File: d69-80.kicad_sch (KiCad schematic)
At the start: 163 parts, among them SW1 SW_Push, SW10 SW_Push, SW101 SW_SPST, SW11 SW_Push, SW12 SW_Push, SW13 SW_Push, SW14 SW_Push, SW15 SW_Push, SW16 SW_Push, SW17 SW_Push, SW18 SW_Push, SW19 SW_Push, SW2 SW_Push, SW20 SW_Push, SW21 SW_Push, SW22 SW_Push, SW23 SW_Push, SW24 SW_Push, SW25 SW_Push, SW26 SW_Push, SW27 SW_Push, SW28 SW_Push, SW29 SW_Push, SW3 SW_Push, SW30 SW_Push, SW31 SW_Push, SW32 SW_Push, SW33 SW_Push, SW34 SW_Push, SW35 SW_Push, SW36 SW_Push, SW37 SW_Push, SW38 SW_Push, SW39 SW_Push, SW4 SW_Push, SW40 SW_Push, SW41 SW_Push, SW42 SW_Push, SW43 SW_Push, SW44 SW_Push, SW45 SW_Push, SW46 SW_Push, SW47 SW_Push, SW48 SW_Push, SW49 SW_Push, SW5 SW_Push, SW50 SW_Push, SW51 SW_Push, SW52 SW_Push, SW53 SW_Push, SW54 SW_Push, SW55 SW_Push, SW56 SW_Push, SW57 SW_Push, SW58 SW_Push, SW59 SW_Push, SW6 SW_Push, SW60 SW_Push, SW61 SW_Push, SW62 SW_Push, SW63 SW_Push, SW64 SW_Push, SW65 SW_Push, SW66 SW_Push, SW67 SW_Push, SW68 SW_Push, SW69 SW_Push, SW7 SW_Push, SW70 SW_Push, SW71 SW_Push, SW72 SW_Push, SW73 SW_Push, SW74 SW_Push, SW75 SW_Push, SW76 SW_Push, SW77 SW_Push, SW78 SW_Push, SW79 SW_Push, SW8 SW_Push, SW80 SW_Push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

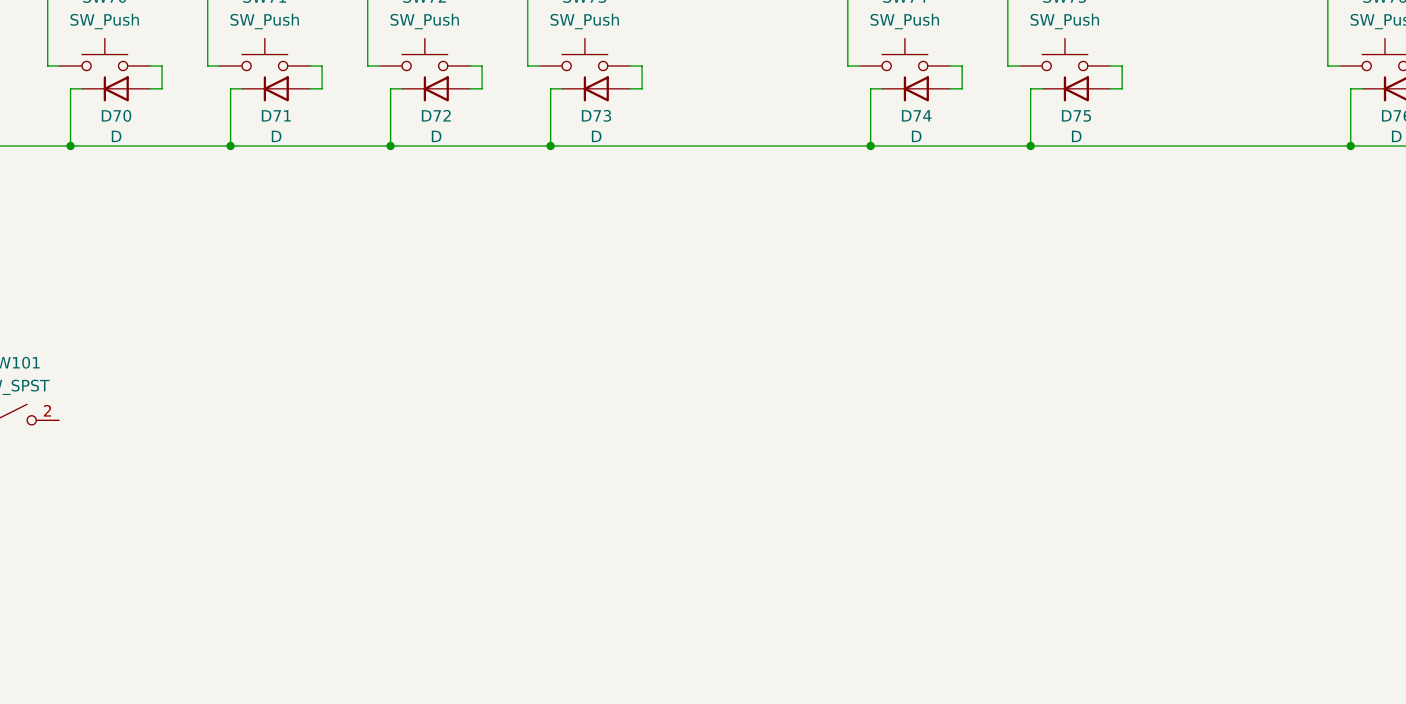
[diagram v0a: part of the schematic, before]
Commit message: adds mcu and io-expander, initial wiring
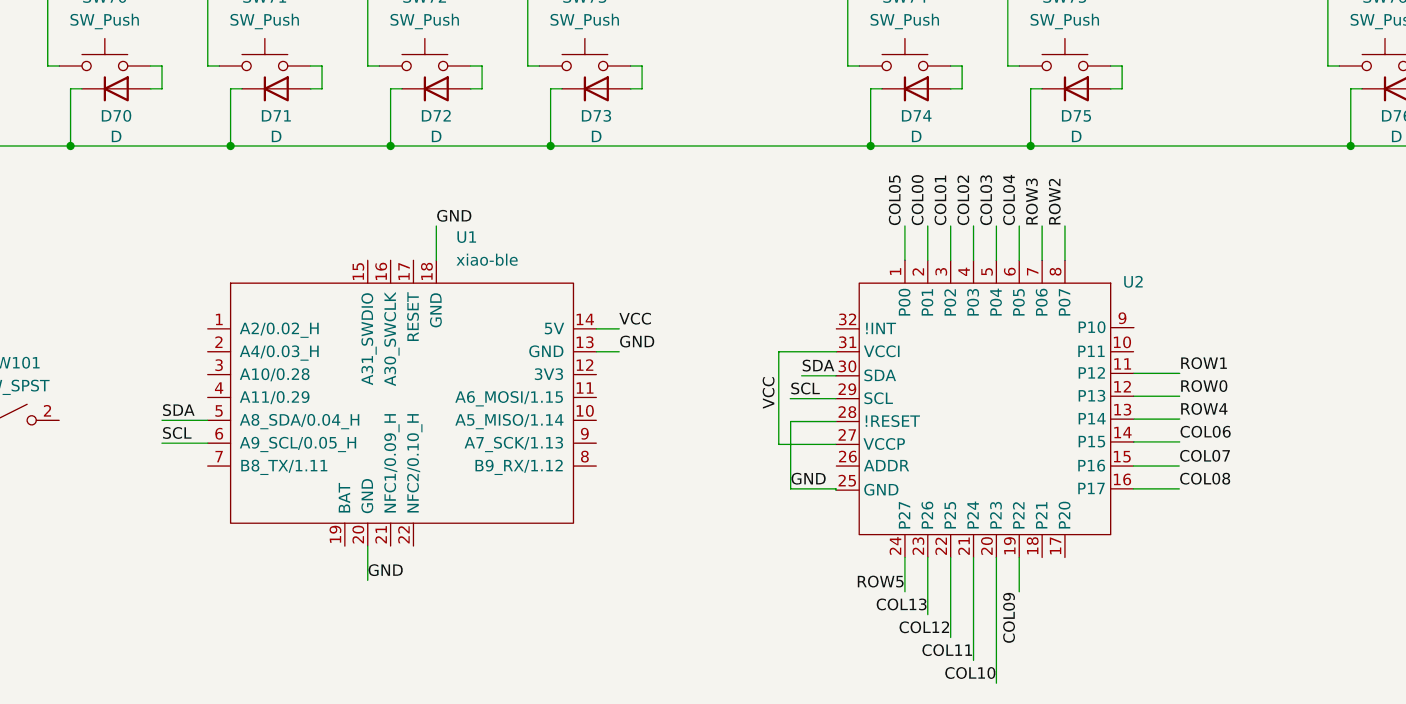
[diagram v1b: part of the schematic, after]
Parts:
- added U1: xiao-ble, Library:xiao-ble-smd-cutout, symbol Library:xiao-ble
- added U2: ~, Library:QFN-32_EP_5x5_Pitch0.5mm, symbol Library:TCA6424
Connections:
- net COL00: now also U2.2 (P01)
- net COL01: now also U2.3 (P02)
- net COL02: now also U2.4 (P03)
- net COL03: now also U2.5 (P04)
- net COL04: now also U2.6 (P05)
- net COL05: now also U2.1 (P00)
- net COL06: now also U2.14 (P15)
- net COL07: now also U2.15 (P16)
- net COL08: now also U2.16 (P17)
- net COL09: now also U2.19 (P22)
- net COL10: now also U2.20 (P23)
- net COL11: now also U2.21 (P24)
- net COL12: now also U2.22 (P25)
- net COL13: now also U2.23 (P26)
- net ROW0: now also U2.12 (P13)
- net ROW1: now also U2.11 (P12)
- net ROW2: now also U2.8 (P07)
- net ROW3: now also U2.7 (P06)
- net ROW4: now also U2.13 (P14)
- net ROW5: now also U2.24 (P27)
- new net GND: U1.13 (GND), U1.18 (GND), U1.20 (GND), U2.25 (GND), U2.28 (!RESET)
- new net SCL: U1.6 (A9_SCL/0.05_H), U2.29 (SCL)
- new net SDA: U1.5 (A8_SDA/0.04_H), U2.30 (SDA)
- new net VCC: U1.14 (5V), U2.27 (VCCP), U2.31 (VCCI)

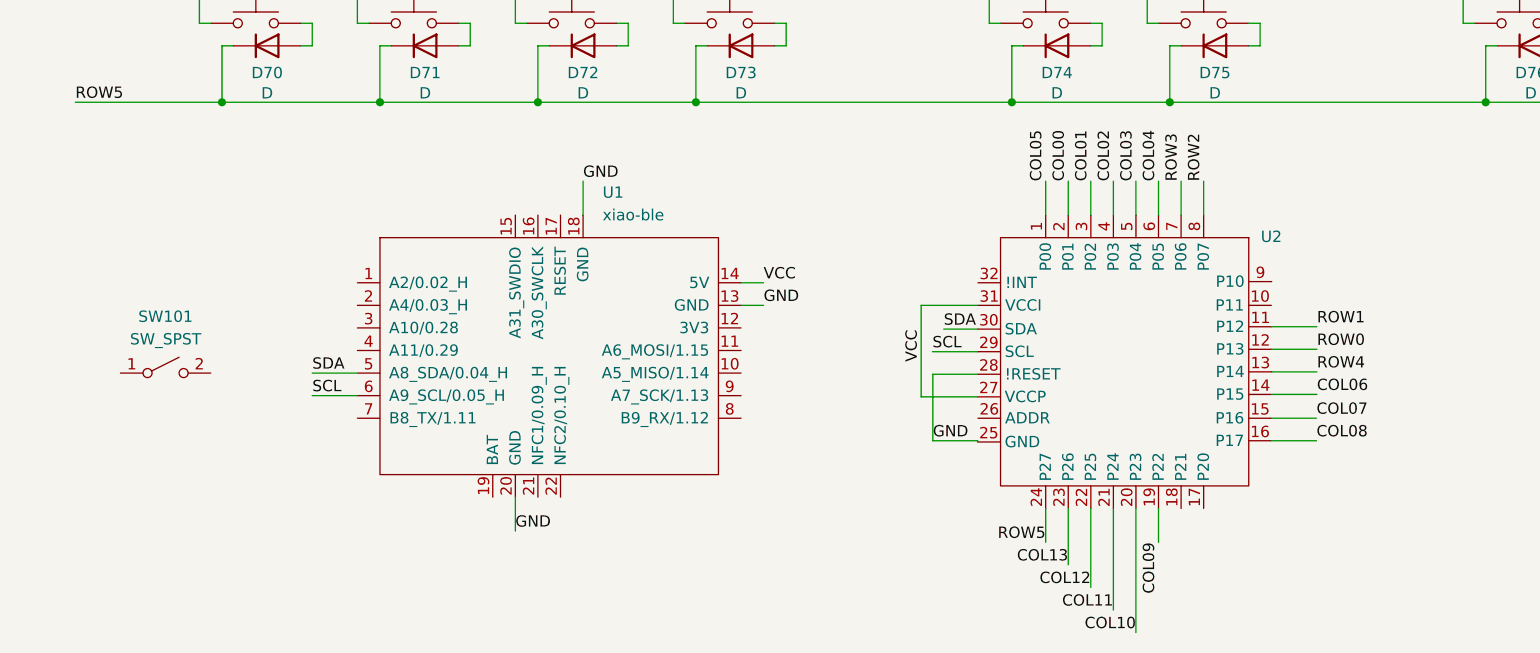
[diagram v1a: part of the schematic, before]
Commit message: adds leds, connects switch and some cleanup
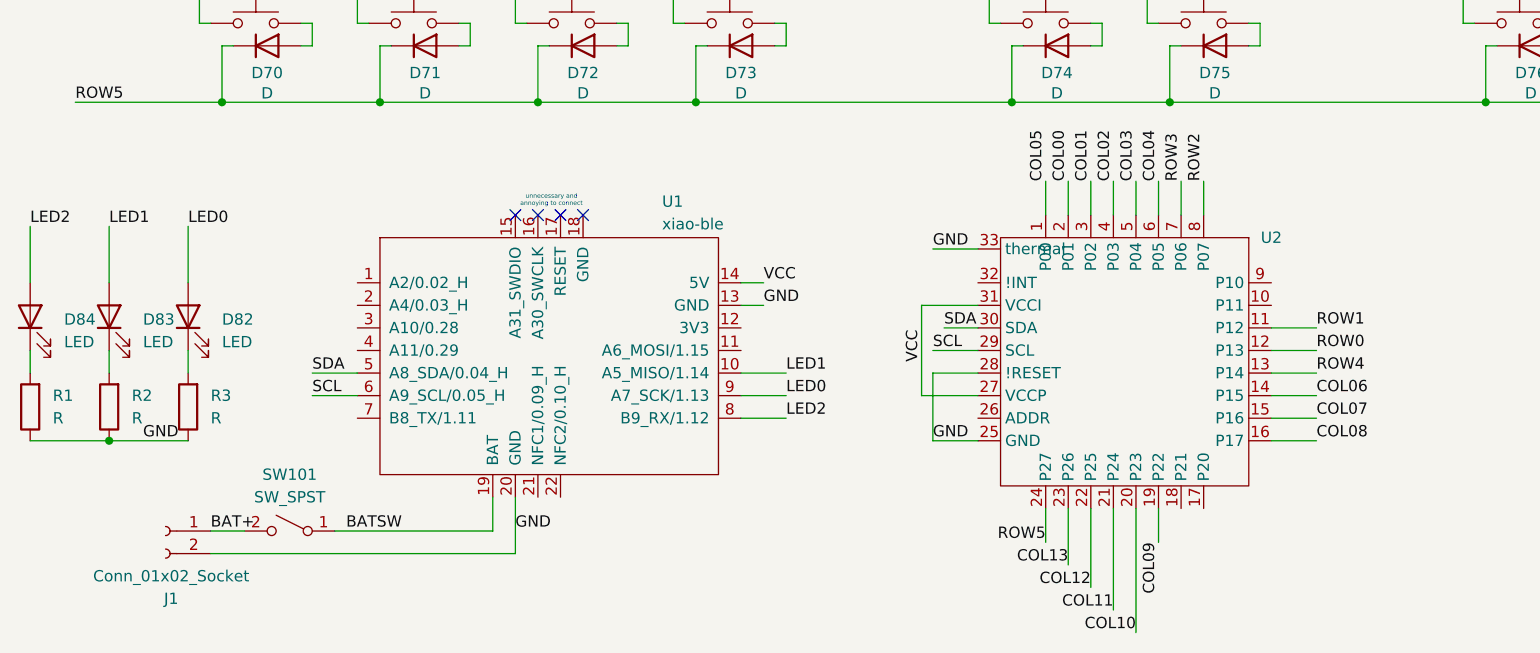
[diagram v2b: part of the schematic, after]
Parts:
- added D82, D83, D84: LED, LED_SMD:LED_0603_1608Metric_Pad1.05x0.95mm_HandSolder, symbol Device:LED
- added J1: Conn_01x02_Socket, Connector_JST:JST_XH_B2B-XH-AM_1x02_P2.50mm_Vertical, symbol Connector:Conn_01x02_Socket
- added R1, R2, R3: R, Resistor_SMD:R_0603_1608Metric_Pad0.98x0.95mm_HandSolder, symbol Device:R
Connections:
- net GND: now also U2.33 (thermal), J1.2 (Pin_2), R1.1, R2.1, R3.1; no longer U1.18 (GND)
- net LED1: now reaches U1.10 (A5_MISO/1.14)
- net LED1: now also D83.2 (A)
- net BATSW: now reaches U1.19 (BAT)
- net BATSW: now also SW101.1 (A)
- net LED2: now reaches U1.8 (B9_RX/1.12)
- net LED2: now also D84.2 (A)
- net LED0: now reaches U1.9 (A7_SCK/1.13)
- net LED0: now also D82.2 (A)
- net BAT+: now reaches SW101.2 (B)
- net BAT+: now also J1.1 (Pin_1)
- new net: D82.1 (K), R3.2
- new net: D83.1 (K), R2.2
- new net: D84.1 (K), R1.2
- no-connect marks 0 -> 4
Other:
- note added: "unnecessary and annoying to connect"
- moved on the sheet: SW101

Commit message: Add I2C pullups (oops), switch to wakeup switch from battery cutoff
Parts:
- added R4, R5: R, Resistor_SMD:R_0603_1608Metric_Pad0.98x0.95mm_HandSolder, symbol Device:R
- SW101: footprint Button_Switch_SMD:SW_DIP_SPSTx01_Slide_9.78x4.72mm_W8.61mm_P2.54mm -> Library:combo
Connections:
- net BAT+: now also U1.19 (BAT); no longer SW101.2 (B)
- net GND: now also SW101.1 (A)
- net SCL: now also R5.2
- net SDA: now also R4.1
- net VCC: now also R4.2, R5.1
- net BOOT: now reaches U1.7 (B8_TX/1.11)
- net BOOT: now also SW101.2 (B)
- removed net BATSW: SW101.1 (A), U1.19 (BAT)
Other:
- moved on the sheet: J1, SW101, U2

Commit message: drc rules and cleanup
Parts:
- SW1, SW15: footprint PCM_Switch_Keyboard_Hotswap_Kailh:SW_Hotswap_Kailh_Choc_V1_1.00u -> PCM_Switch_Keyboard_Hotswap_Kailh:SW_Hotswap_Kailh_Choc_V1_1.00u_mod3
- SW10, SW11, SW12, SW13, SW14, SW16, SW17, SW18, SW19, SW20, SW21, SW22, SW23, SW24, SW25, SW26, SW27, SW30, SW31, SW32, SW33, SW34, SW35, SW36, SW37, SW38, SW39, SW40, SW41, SW44, SW45, SW46, SW47, SW48, SW49, SW50, SW51, SW52, SW53, SW54, SW55, SW56, SW57, SW58, SW59, SW6, SW60, SW61, SW62, SW63, SW64, SW65, SW66, SW67, SW68, SW7, SW70, SW71, SW72, SW73, SW76, SW77, SW78, SW79, SW8, SW80, SW81, SW9: footprint PCM_Switch_Keyboard_Hotswap_Kailh:SW_Hotswap_Kailh_Choc_V1_1.00u -> PCM_Switch_Keyboard_Hotswap_Kailh:SW_Hotswap_Kailh_Choc_V1_1.00u_mod1
- SW2, SW3, SW4, SW5: footprint PCM_Switch_Keyboard_Hotswap_Kailh:SW_Hotswap_Kailh_Choc_V1_1.00u -> PCM_Switch_Keyboard_Hotswap_Kailh:SW_Hotswap_Kailh_Choc_V1_1.00u_mod2
- SW28, SW43, SW69: footprint PCM_Switch_Keyboard_Hotswap_Kailh:SW_Hotswap_Kailh_Choc_V1_1.50u -> PCM_Switch_Keyboard_Hotswap_Kailh:SW_Hotswap_Kailh_Choc_V1_1.50u_mod1
- SW29: footprint PCM_Switch_Keyboard_Hotswap_Kailh:SW_Hotswap_Kailh_Choc_V1_1.25u -> PCM_Switch_Keyboard_Hotswap_Kailh:SW_Hotswap_Kailh_Choc_V1_1.25u_mod1
- SW42: footprint PCM_Switch_Keyboard_Hotswap_Kailh:SW_Hotswap_Kailh_Choc_V1_ISOEnter -> PCM_Switch_Keyboard_Hotswap_Kailh:SW_Hotswap_Kailh_Choc_V1_ISOEnter_custom
- SW74, SW75: footprint PCM_Switch_Keyboard_Hotswap_Kailh:SW_Hotswap_Kailh_Choc_V1_2.00u -> PCM_Switch_Keyboard_Hotswap_Kailh:SW_Hotswap_Kailh_Choc_V1_2.00u_mod1
- renumbered D82 to D102, D83 to D103, D84 to D104
